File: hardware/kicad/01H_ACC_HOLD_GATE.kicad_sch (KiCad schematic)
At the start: 15 parts, among them Q912 MMBT5551, Q913 MMBT5551, U911 140356145000 HOLD OPTICAL

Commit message: fix(power): source ACC startup from VIN and remove ACC-only buck EN overstress path
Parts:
- added Q914: PMBT5551,215, Tripmaster:Q_SOT23_1B2E3C, symbol TripTracer_V1:PMBT5551_ACC
- added Q915: MMBT5401-7-F, Tripmaster:Q_SOT23_1B2E3C, symbol TripTracer_V1:MMBT5401_ACC
- added R922: 10k 1% 0.5W, Tripmaster:R_1206_3216, symbol Tripmaster_Sym:R
- added R923: 10k 1% 0.5W ACC, Tripmaster:R_1206_3216, symbol Tripmaster_Sym:R
- added R924: 4.7k 1%, Tripmaster:R_1206_3216, symbol Tripmaster_Sym:R
- D911: value BAT54WS EN OR -> BAT54WS negative ACC clamp
- R911: value 100k ACC LIMIT -> 33k 1% VIN LIMIT
- R912: value 47k ACC BIAS BLEED -> 2.2k 1% E-B OFF
- R913: value 100k EN PULLDOWN -> 10k 1% EN OFF
- R915: value 100k HOLD VIN LIMIT -> 33k 1% HOLD VIN
- R916: value 100k ACC NPN base feed -> 100k ACC sense
- R917: value 47k ACC output pulldown -> 47k output bleed
- R918: value 100k base leak pull-down -> 100k base OFF
- R919: value 22k first collector pull-up -> 22k first pull-up
- R920: value 22k second base feed -> 22k second base
- R921: value 10k ACC output pull-up -> 10k output pull-up
- U911: value 140356145000 HOLD OPTICAL -> 140356145000 HOLD
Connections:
- net ACC_DRIVE_5V: now also R917.2, R921.1; no longer R917.1, R921.2
- net ACC_INV_N: now also R919.1; no longer R919.2
- net ACC_PROTECTED_IN: now also R923.1; no longer R911.1
- net ACC_Q912_BASE: now also R918.2; no longer R918.1
- net BUCK_ENABLE: now also R911.2, R913.2; no longer D911.2 (K), R913.1
- net GND: now also D911.1 (A), R913.1, R917.1, R918.1, Q914.2 (E), R924.1; no longer R912.2, R913.2, R917.2, R918.2
- net HV_PROTECTED_AFTER_EFUSE: now also R912.2, R915.2, Q915.2 (E); no longer R915.1
- net V3V3_SYS: now also R919.2, R921.2; no longer R919.1, R921.1
- net VIN_HOLD_BIAS: now also R915.1; no longer R915.2
- removed net ACC_EN_BIAS: D911.1 (A), R911.2, R912.1
- new net ACC_START_BASE: D911.2 (K), Q914.1 (B), R923.2, R924.2
- new net ACC_START_PNP_BASE: Q915.1 (B), R912.1, R922.2
- new net ACC_START_SINK: Q914.3 (C), R922.1
- new net ACC_START_VIN: Q915.3 (C), R911.1
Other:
- note added: "ACC SENSE: independent original Q912/Q913 double inversion; output is 3V3 despite historical net name."
- note added: "ACC STARTUP: ACC only drives Q914 base. Q915 sources EN exclusively from buck VIN; no 3V3 startup dependency."
- note added: "LAB ONLY: check hot leakage, timing overlap at ACC fall, VIN/EN disconnect slew, reverse inputs and vehicle pulses. No vehicle approval."
- note added: "MCU HOLD: existing 555 grant AND MCU request; opto output draws only from VIN."
- note removed: "CRITICAL: photocoupler U911 VCEO, CTR at -40C and LED current; Q912/Q913 BJT beta, VBE at hot/cold, ACC base resistor leakage, exact pinout/footprint, 9V and 30V thresholds, ACC transient protection, 01C 555 proper trigger and 3V3 power, power-on behavior ALL REQUIRE VERIFICATION. DO NOT FABRICATE."
- note removed: "PROTOTYPE: ACC resistor divider + D911 BAT54 (A=1, K=2) starts EN independent of 5V. Opto U911 powered by VIN permits post-ACC MCU_HOLD only during independent 555 grant. Q912/Q913 double NPN stage generates non-inverted 3V3 ACC sense for the existing 555 falling-edge trigger; no CTR assumption."
- title: TripTracer - ACC MCU HOLD COLD BOOT GATE -> TripTracer ACC startup referenced to buck VIN / bounded MCU HOLD

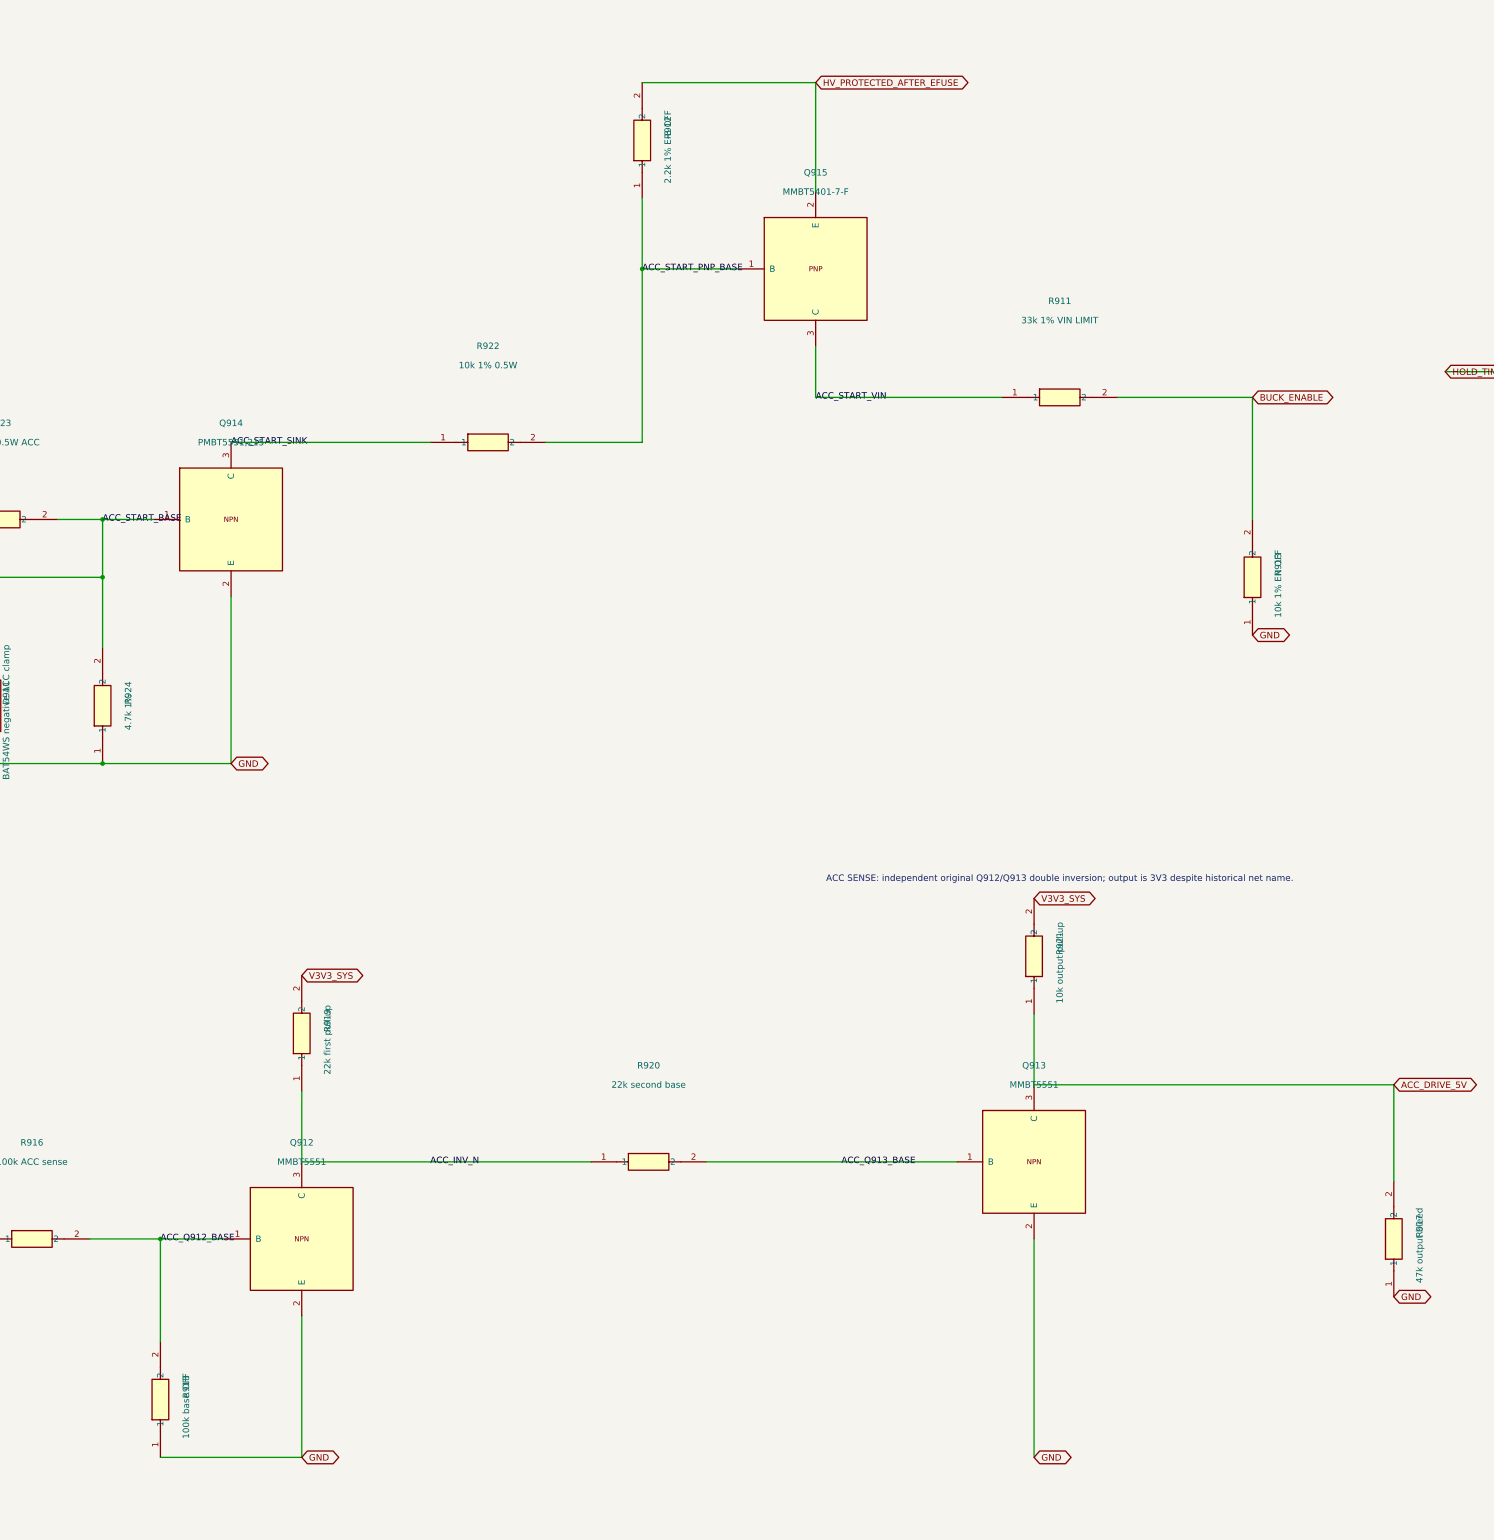
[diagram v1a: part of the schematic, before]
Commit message: fix(power): preserve top-to-bottom resistor pin numbering in VIN startup drawing
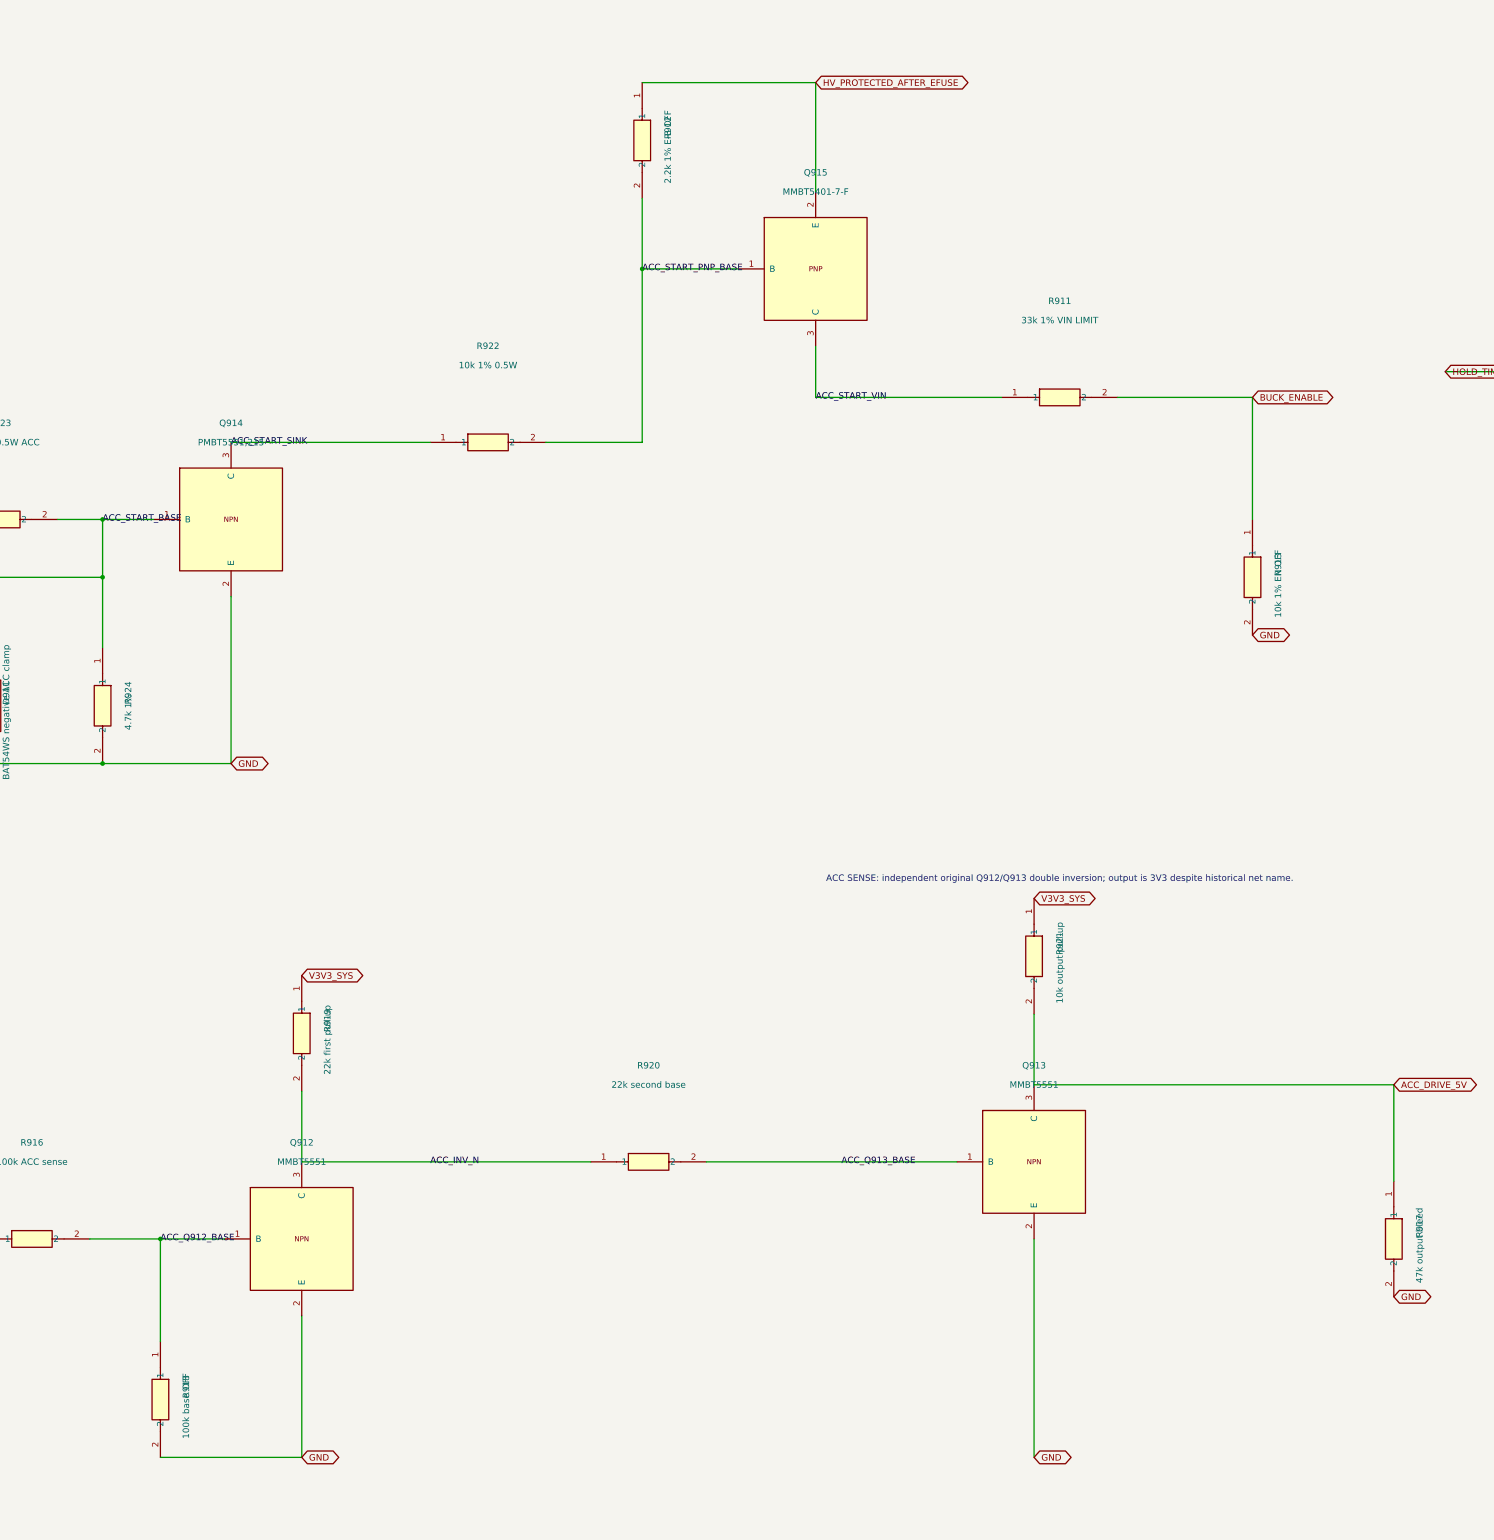
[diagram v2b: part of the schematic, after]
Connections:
- net ACC_DRIVE_5V: now also R917.1, R921.2; no longer R917.2, R921.1
- net ACC_INV_N: now also R919.2; no longer R919.1
- net ACC_Q912_BASE: now also R918.1; no longer R918.2
- net ACC_START_BASE: now also R924.1; no longer R924.2
- net ACC_START_PNP_BASE: now also R912.2; no longer R912.1
- net BUCK_ENABLE: now also R913.1; no longer R913.2
- net GND: now also R913.2, R917.2, R918.2, R924.2; no longer R913.1, R917.1, R918.1, R924.1
- net HV_PROTECTED_AFTER_EFUSE: now also R912.1; no longer R912.2
- net V3V3_SYS: now also R919.1, R921.1; no longer R919.2, R921.2
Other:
- moved on the sheet: R912, R913, R917, R918, R919, R921, R924
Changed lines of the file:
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@@
 (pin "2")
 (instances (project "TripTracer_V1" (path "/a26d9b0c-7f10-4e5a-a65f-000000000064/a26d9b0c-7f10-4e5a-a65f-000000000065" (reference "R923") (unit 1)))))
-(symbol (lib_id "Tripmaster_Sym:R") (at 74.93 171.45 90) (unit 1) (in_bom yes) (on_board yes) (dnp no)
+(symbol (lib_id "Tripmaster_Sym:R") (at 74.93 171.45 270) (unit 1) (in_bom yes) (on_board yes) (dnp no)
 (property "Reference" "R924" (at 80.01 168.91 0) (effects (font (size 1.27 1.27))))
 (property "Value" "4.7k 1%" (at 80.01 172.72 0) (effects (font (size 1.27 1.27))))
@@
 (pin "2")
 (instances (project "TripTracer_V1" (path "/a26d9b0c-7f10-4e5a-a65f-000000000064/a26d9b0c-7f10-4e5a-a65f-000000000065" (reference "R922") (unit 1)))))
-(symbol (lib_id "Tripmaster_Sym:R") (at 181.61 59.69 90) (unit 1) (in_bom yes) (on_board yes) (dnp no)
+(symbol (lib_id "Tripmaster_Sym:R") (at 181.61 59.69 270) (unit 1) (in_bom yes) (on_board yes) (dnp no)
 (property "Reference" "R912" (at 186.69 57.15 0) (effects (font (size 1.27 1.27))))
 (property "Value" "2.2k 1% E-B OFF" (at 186.69 60.96 0) (effects (font (size 1.27 1.27))))
@@
 (pin "2")
 (instances (project "TripTracer_V1" (path "/a26d9b0c-7f10-4e5a-a65f-000000000064/a26d9b0c-7f10-4e5a-a65f-000000000065" (reference "R911") (unit 1)))))
-(symbol (lib_id "Tripmaster_Sym:R") (at 302.26 146.05 90) (unit 1) (in_bom yes) (on_board yes) (dnp no)
+(symbol (lib_id "Tripmaster_Sym:R") (at 302.26 146.05 270) (unit 1) (in_bom yes) (on_board yes) (dnp no)
 (property "Reference" "R913" (at 307.34 143.51 0) (effects (font (size 1.27 1.27))))
 (property "Value" "10k 1% EN OFF" (at 307.34 147.32 0) (effects (font (size 1.27 1.27))))
@@
 (pin "2")
 (instances (project "TripTracer_V1" (path "/a26d9b0c-7f10-4e5a-a65f-000000000064/a26d9b0c-7f10-4e5a-a65f-000000000065" (reference "R916") (unit 1)))))
-(symbol (lib_id "Tripmaster_Sym:R") (at 86.36 308.61 90) (unit 1) (in_bom yes) (on_board yes) (dnp no)
+(symbol (lib_id "Tripmaster_Sym:R") (at 86.36 308.61 270) (unit 1) (in_bom yes) (on_board yes) (dnp no)
 (property "Reference" "R918" (at 91.44 306.07 0) (effects (font (size 1.27 1.27))))
 (property "Value" "100k base OFF" (at 91.44 309.88 0) (effects (font (size 1.27 1.27))))
@@
 (pin "3")
 (instances (project "TripTracer_V1" (path "/a26d9b0c-7f10-4e5a-a65f-000000000064/a26d9b0c-7f10-4e5a-a65f-000000000065" (reference "Q912") (unit 1)))))
-(symbol (lib_id "Tripmaster_Sym:R") (at 114.3 236.22 90) (unit 1) (in_bom yes) (on_board yes) (dnp no)
+(symbol (lib_id "Tripmaster_Sym:R") (at 114.3 236.22 270) (unit 1) (in_bom yes) (on_board yes) (dnp no)
 (property "Reference" "R919" (at 119.38 233.68 0) (effects (font (size 1.27 1.27))))
 (property "Value" "22k first pull-up" (at 119.38 237.49 0) (effects (font (size 1.27 1.27))))
@@
 (pin "3")
 (instances (project "TripTracer_V1" (path "/a26d9b0c-7f10-4e5a-a65f-000000000064/a26d9b0c-7f10-4e5a-a65f-000000000065" (reference "Q913") (unit 1)))))
-(symbol (lib_id "Tripmaster_Sym:R") (at 259.08 220.98 90) (unit 1) (in_bom yes) (on_board yes) (dnp no)
+(symbol (lib_id "Tripmaster_Sym:R") (at 259.08 220.98 270) (unit 1) (in_bom yes) (on_board yes) (dnp no)
 (property "Reference" "R921" (at 264.16 218.44 0) (effects (font (size 1.27 1.27))))
 (property "Value" "10k output pull-up" (at 264.16 222.25 0) (effects (font (size 1.27 1.27))))
@@
 (pin "2")
 (instances (project "TripTracer_V1" (path "/a26d9b0c-7f10-4e5a-a65f-000000000064/a26d9b0c-7f10-4e5a-a65f-000000000065" (reference "R921") (unit 1)))))
-(symbol (lib_id "Tripmaster_Sym:R") (at 330.2 276.86 90) (unit 1) (in_bom yes) (on_board yes) (dnp no)
+(symbol (lib_id "Tripmaster_Sym:R") (at 330.2 276.86 270) (unit 1) (in_bom yes) (on_board yes) (dnp no)
 (property "Reference" "R917" (at 335.28 274.32 0) (effects (font (size 1.27 1.27))))
 (property "Value" "47k output bleed" (at 335.28 278.13 0) (effects (font (size 1.27 1.27))))

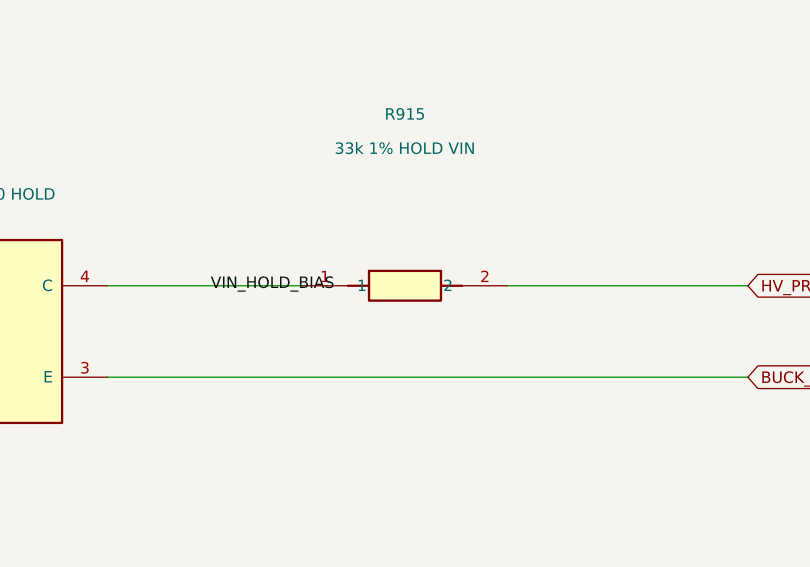
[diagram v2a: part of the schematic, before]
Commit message: fix(power): retain original VIN-side pin 1 on optical HOLD feed resistor
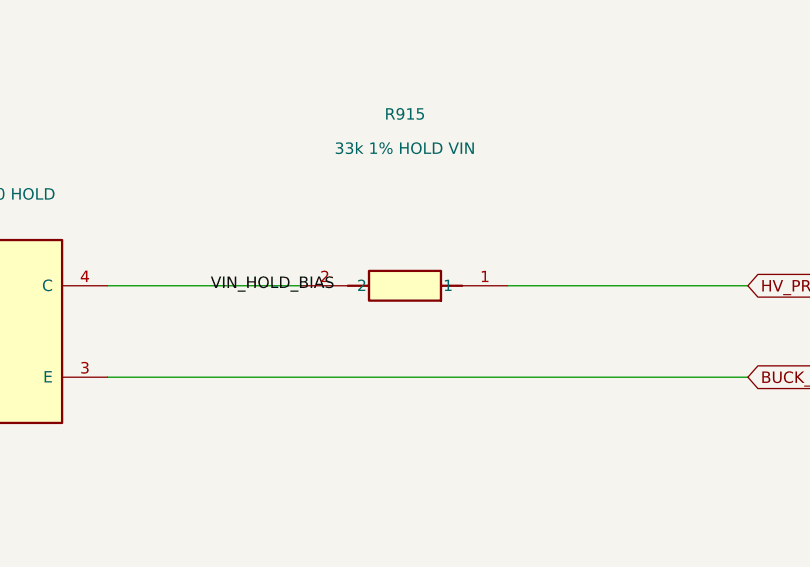
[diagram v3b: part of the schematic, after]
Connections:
- net HV_PROTECTED_AFTER_EFUSE: now also R915.1; no longer R915.2
- net VIN_HOLD_BIAS: now also R915.2; no longer R915.1
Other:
- moved on the sheet: R915
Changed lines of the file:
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@@
 (pin "2")
 (instances (project "TripTracer_V1" (path "/a26d9b0c-7f10-4e5a-a65f-000000000064/a26d9b0c-7f10-4e5a-a65f-000000000065" (reference "R914") (unit 1)))))
-(symbol (lib_id "Tripmaster_Sym:R") (at 477.52 105.41 0) (unit 1) (in_bom yes) (on_board yes) (dnp no)
+(symbol (lib_id "Tripmaster_Sym:R") (at 477.52 105.41 180) (unit 1) (in_bom yes) (on_board yes) (dnp no)
 (property "Reference" "R915" (at 477.52 86.36 0) (effects (font (size 1.27 1.27))))
 (property "Value" "33k 1% HOLD VIN" (at 477.52 90.17 0) (effects (font (size 1.27 1.27))))

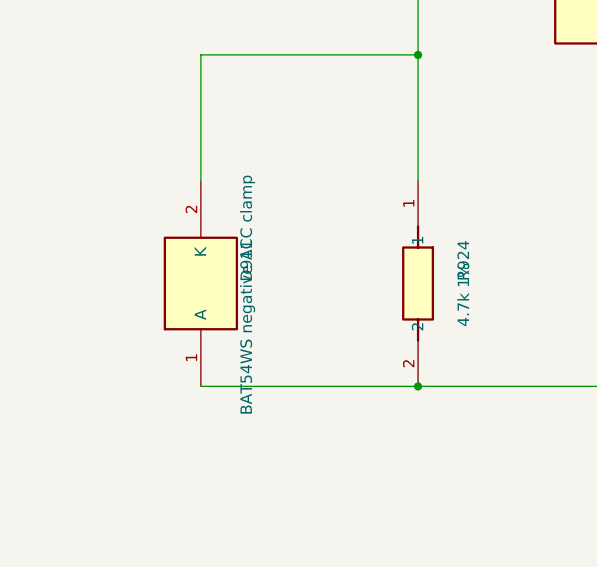
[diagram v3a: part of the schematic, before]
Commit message: fix(power): map reused ACC negative clamp cathode to SOD323 pad 1
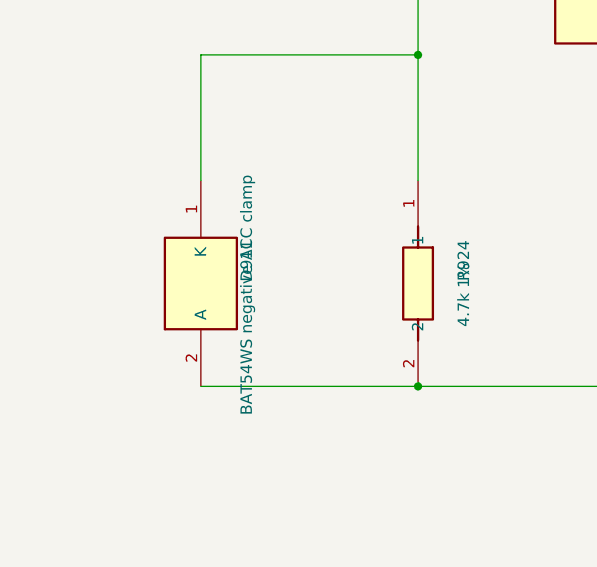
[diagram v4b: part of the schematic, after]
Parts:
- D911: symbol TripTracer_V1:BAT54WS_EN -> TripTracer_V1:BAT54WS_CLAMP
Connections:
- net ACC_START_BASE: now also D911.1 (K); no longer D911.2 (K)
- net GND: now also D911.2 (A); no longer D911.1 (A)
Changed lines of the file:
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@@
 (pin "2")
 (instances (project "TripTracer_V1" (path "/a26d9b0c-7f10-4e5a-a65f-000000000064/a26d9b0c-7f10-4e5a-a65f-000000000065" (reference "R913") (unit 1)))))
-(symbol (lib_id "TripTracer_V1:BAT54WS_EN") (at 50.8 171.45 90) (unit 1) (in_bom yes) (on_board yes) (dnp no)
+(symbol (lib_id "TripTracer_V1:BAT54WS_CLAMP") (at 50.8 171.45 90) (unit 1) (in_bom yes) (on_board yes) (dnp no)
 (property "Reference" "D911" (at 55.88 168.91 0) (effects (font (size 1.27 1.27))))
 (property "Value" "BAT54WS negative ACC clamp" (at 55.88 172.72 0) (effects (font (size 1.27 1.27))))
